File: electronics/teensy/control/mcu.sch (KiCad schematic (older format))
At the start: 23 parts, among them J23 USB_B, J24 EXT, J25 EXT, Q4 SI2301CDS-T1-E3, U16 Cetus_J1B1211CCD, U17 CY7C64225, U18 LM810M3-4.63, U19 Teensy_4.1

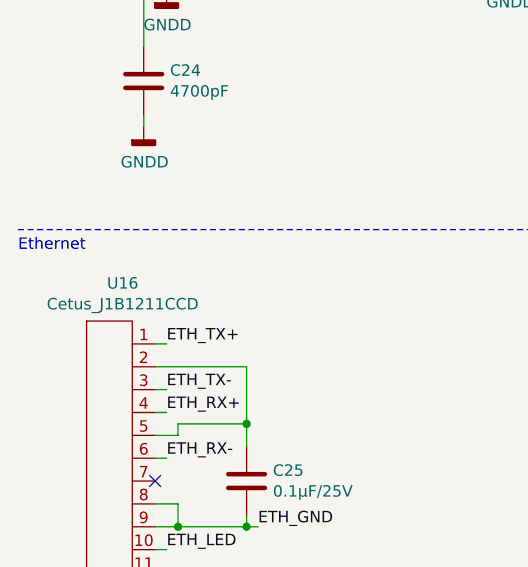
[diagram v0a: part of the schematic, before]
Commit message: Add ResourceLock tests.
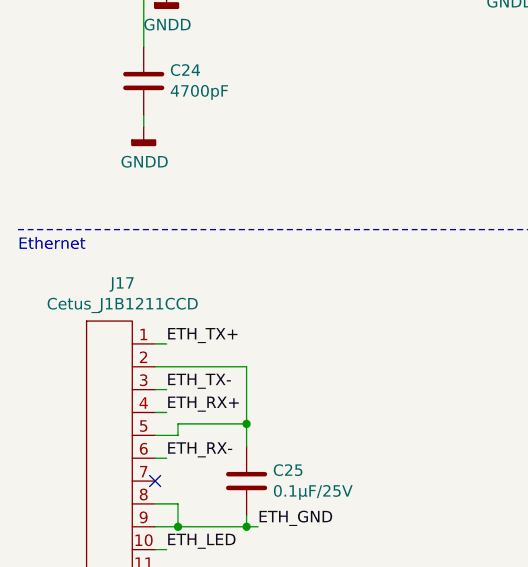
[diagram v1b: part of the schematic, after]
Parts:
- renumbered U16 to J17
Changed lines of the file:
@@
 $EndComp
 $Comp
-L CNC:Cetus_J1B1211CCD U16
+L CNC:Cetus_J1B1211CCD J17
 U 1 1 6195AE16
 P 900 4350
-F 0 "U16" H 958 4415 50  0000 C CNN
+F 0 "J17" H 958 4415 50  0000 C CNN
 F 1 "Cetus_J1B1211CCD" H 958 4324 50  0000 C CNN
 F 2 "cnc:Cetus J1B1211CCD" H 900 4350 50  0001 C CNN

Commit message: Add gerber files
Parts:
- added R44: 20k, Resistor_SMD:R_0805_2012Metric, symbol Device:R
- added R49, R50, R69, R70, R71: 1k, Resistor_SMD:R_0805_2012Metric, symbol Device:R
- R59: value 1k -> 10k
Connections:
- net GNDD: now also R44.2, R71.2
- net USB_UART_CTS: now also R69.1; no longer U17.21 (CTS)
- net USB_UART_RTS: now also R50.1; no longer U17.24 (RTS)
- net USB_UART_RX: now also R70.1; no longer U17.23 (RxD)
- net USB_UART_TX: now also R49.1; no longer U17.4 (TxD)
- net at R59.1, U17.7 (VBUS): now also R44.1
- net PIN_20: no longer names the net of J25.3 (Pin_3)
- net USB_UART_DSR: no longer names the net of U19.38 (38/A14)
- net USB_UART_DSR: no longer U17.8 (DSR)
- net USB_UART_DTR: no longer names the net of U19.36 (36/CS/PWM)
- net USB_UART_DTR: no longer U17.5 (DTR)
- net USB_UART_RESET: no longer names the net of U19.37 (37/CS/PWM)
- net USB_UART_RESET: no longer U17.6 (Reset)
- net USB_UART_WAKE: no longer names the net of U19.40 (40/A16)
- net USB_UART_WAKE: no longer U17.22 (WAKE)
- new net: R49.2, U17.4 (TxD)
- new net: R70.2, U17.23 (RxD)
- new net: R50.2, U17.24 (RTS)
- new net: R69.2, U17.21 (CTS)
- new net: R71.1, U17.22 (WAKE)
- new net: U17.5 (DTR), U17.8 (DSR)
- no-connect marks 12 -> 18
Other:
- moved on the sheet: C24, D3, D4, D5, D6, J23, R59, R60, R61, R62, R63, R64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
